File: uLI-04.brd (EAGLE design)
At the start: 57 x 38.5 mm, 39 parts, among them IC1 PIC18F14K50-I/SS, IC2 ADM2483, IC3 MCP130T, IC4 78L05F, J1 PICPROG2-V, J5 WEBP6-4, J6 WEBP6-4, J7 WEBP6-4, Q1 12.00 MHz, T1 IRF7306, X1 MINI-USB_SHIELD4P-USB-SPEC, X2 ARK1550/2_S

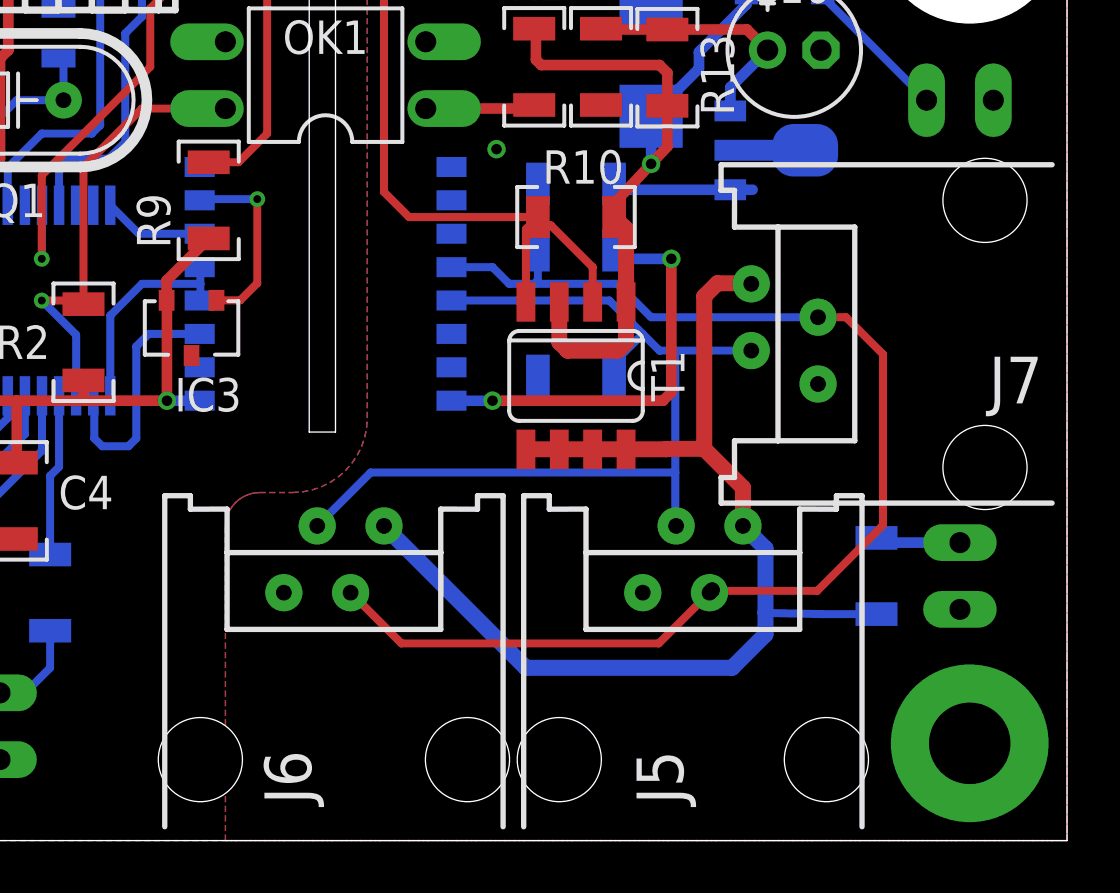
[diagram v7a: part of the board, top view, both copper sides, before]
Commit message: 6-4 > 6-6, ploska J5.
 * Konektory WEBP 6-4 nahrazeny za WEBP 6-6. Close #3.
 * Pajeci ploska pobliz J5 odstranena. Close 2.
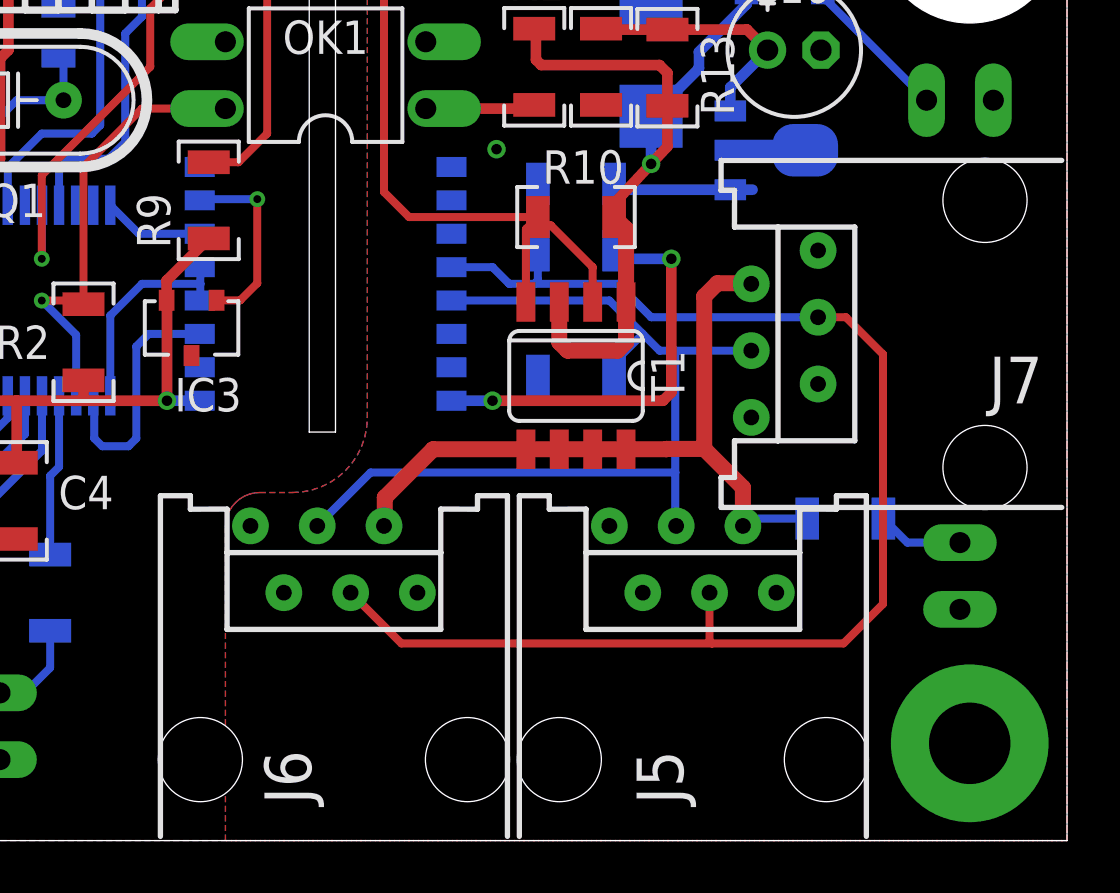
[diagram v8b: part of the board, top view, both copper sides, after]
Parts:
- J5, J6, J7: value WEBP6-4 -> WEBP6; device con-malina:WEBP6-4_SHORT -> con-malina:WEBP6-6_SPEC2
- moved R11 2.48 mm to (50.6, 14.2), turned to 0 degrees
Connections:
- new net N$11: J6.1
- new net N$12: J5.6
- new net N$13: J5.1
- new net N$14: J7.6
- new net N$15: J7.1
- new net N$8: J6.6
- net +NAP: now also J5.5, J6.5, J7.5; no longer J5.4, J6.4, J7.4
- net BUS_A: now also J5.4, J6.4, J7.4; no longer J5.3, J6.3, J7.3
- net BUS_B: now also J5.3, J6.3, J7.3; no longer J5.2, J6.2, J7.2
- net GNDINT: now also J5.2, J6.2, J7.2; no longer J5.1, J6.1, J7.1
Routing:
- net +NAP: track 44.1 -> 27.9 mm
- net BUS_A: track 48.7 -> 52.4 mm, vias 1 -> 0
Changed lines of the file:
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@@
 <attribute name="VALUE" x="46.339" y="34.0195" size="1.27" layer="27" ratio="10"/>
 </element>
-<element name="J5" library="con-malina" package="WEBP6-4_SHORT" value="WEBP6-4" x="44.7675" y="5.08" smashed="yes">
+<element name="J5" library="con-malina" package="WEBP6-6_SPEC2" value="WEBP6" x="44.7675" y="5.08" smashed="yes">
 <attribute name="NAME" x="44.4015" y="3.389" size="1.778" layer="25" rot="R90"/>
 </element>
-<element name="J6" library="con-malina" package="WEBP6-4_SHORT" value="WEBP6-4" x="31.115" y="5.08" smashed="yes">
+<element name="J6" library="con-malina" package="WEBP6-6_SPEC2" value="WEBP6" x="31.115" y="5.08" smashed="yes">
 <attribute name="NAME" x="30.249" y="3.389" size="1.778" layer="25" rot="R90"/>
 </element>
-<element name="J7" library="con-malina" package="WEBP6-4_SHORT" value="WEBP6-4" x="55.88" y="21.2725" smashed="yes" rot="R90">
+<element name="J7" library="con-malina" package="WEBP6-6_SPEC2" value="WEBP6" x="55.88" y="21.2725" smashed="yes" rot="R90">
 <attribute name="NAME" x="58.071" y="20.4065" size="1.778" layer="25" rot="R180"/>
 </element>
@@
 <attribute name="VALUE" x="58.7375" y="12.065" size="1.27" layer="28" ratio="15" rot="MR270" align="bottom-center"/>
 </element>
-<element name="R11" library="rcl" package="R1206" value="10k" x="51.7525" y="12.065" smashed="yes" rot="MR270">
-<attribute name="NAME" x="50.4825" y="13.335" size="1.27" layer="26" font="vector" ratio="15" rot="MR270"/>
-<attribute name="VALUE" x="50.2925" y="13.835" size="1.27" layer="28" font="vector" ratio="15" rot="MR270"/>
+<element name="R11" library="rcl" package="R1206" value="10k" x="50.565" y="14.2475" smashed="yes" rot="MR0">
+<attribute name="NAME" x="51.835" y="15.5175" size="1.27" layer="26" font="vector" ratio="15" rot="MR0"/>
+<attribute name="VALUE" x="52.335" y="15.7075" size="1.27" layer="28" font="vector" ratio="15" rot="MR0"/>
 </element>
 <element name="R13" library="rcl" package="R1206" value="22R" x="43.8" y="31.4" rot="R270"/>
@@
 <contactref element="X2" pad="2"/>
 <contactref element="LED5" pad="K"/>
-<contactref element="J6" pad="1"/>
-<contactref element="J7" pad="1"/>
-<contactref element="J5" pad="1"/>
+<contactref element="J6" pad="2"/>
+<contactref element="J7" pad="2"/>
+<contactref element="J5" pad="2"/>
 <via x="37.3" y="28.3" extent="1-16" drill="0.4"/>
 </signal>
@@
 <wire x1="38.8725" y1="24.4475" x2="38.8725" y2="23.315" width="0.3048" layer="16"/>
 <wire x1="38.8725" y1="23.315" x2="38.735" y2="23.1775" width="0.3048" layer="16"/>
-<contactref element="J6" pad="3"/>
-<contactref element="J7" pad="3"/>
-<contactref element="J5" pad="3"/>
+<contactref element="J6" pad="4"/>
+<contactref element="J7" pad="4"/>
+<contactref element="J5" pad="4"/>
 <wire x1="49.53" y1="21.9075" x2="43.18" y2="21.9075" width="0.3048" layer="16"/>
 <wire x1="31.75" y1="11.43" x2="33.68" y2="9.5" width="0.3048" layer="1"/>
-<wire x1="45.4025" y1="11.43" x2="43.4725" y2="9.5" width="0.3048" layer="1"/>
-<wire x1="43.4725" y1="9.5" x2="33.68" y2="9.5" width="0.3048" layer="1"/>
-<wire x1="45.4025" y1="11.43" x2="45.5" y2="11.5275" width="0.3048" layer="16"/>
+<wire x1="50.5" y1="9.5" x2="45.5" y2="9.5" width="0.3048" layer="1"/>
+<wire x1="45.5" y1="9.5" x2="33.68" y2="9.5" width="0.3048" layer="1"/>
 <wire x1="49.53" y1="21.73" x2="49.53" y2="21.9075" width="0.3048" layer="16"/>
-<via x="45.5" y="11.5275" extent="1-16" drill="0.6" shape="square"/>
-<wire x1="45.5" y1="11.5275" x2="45.5275" y2="11.5" width="0.3048" layer="1"/>
-<wire x1="45.5275" y1="11.5" x2="49.5" y2="11.5" width="0.3048" layer="1"/>
-<wire x1="49.5" y1="11.5" x2="52" y2="14" width="0.3048" layer="1"/>
-<wire x1="52" y1="14" x2="52" y2="20.5" width="0.3048" layer="1"/>
+<wire x1="52" y1="11" x2="52" y2="20.5" width="0.3048" layer="1"/>
 <wire x1="52" y1="20.5" x2="50.5925" y2="21.9075" width="0.3048" layer="1"/>
 <wire x1="50.5925" y1="21.9075" x2="49.53" y2="21.9075" width="0.3048" layer="1"/>
+<wire x1="50.5" y1="9.5" x2="52" y2="11" width="0.3048" layer="1"/>
+<wire x1="45.4025" y1="11.43" x2="45.4025" y2="9.5975" width="0.3048" layer="1"/>
+<wire x1="45.4025" y1="9.5975" x2="45.5" y2="9.5" width="0.3048" layer="1"/>
 </signal>
 <signal name="BUS_B" class="1">
@@
 <wire x1="41.7725" y1="19.685" x2="41.7725" y2="20.1825" width="0.3048" layer="16"/>
 <wire x1="41.7725" y1="20.1825" x2="42.8625" y2="21.2725" width="0.3048" layer="16"/>
-<contactref element="J6" pad="2"/>
-<contactref element="J7" pad="2"/>
-<contactref element="J5" pad="2"/>
+<contactref element="J6" pad="3"/>
+<contactref element="J7" pad="3"/>
+<contactref element="J5" pad="3"/>
 <wire x1="46.99" y1="20.6375" x2="44.1" y2="20.6375" width="0.3048" layer="16"/>
 <wire x1="44.1" y1="20.6375" x2="43.4975" y2="20.6375" width="0.3048" layer="16"/>
@@
 <contactref element="T1" pad="8"/>
 <contactref element="R11" pad="2"/>
-<wire x1="47.53" y1="10.66" x2="47.53" y2="9.8425" width="0.6096" layer="16"/>
-<wire x1="47.53" y1="9.8425" x2="46.26" y2="8.5725" width="0.6096" layer="16"/>
-<wire x1="51.7525" y1="10.615" x2="49.6675" y2="10.615" width="0.3048" layer="16"/>
-<wire x1="49.6675" y1="10.615" x2="47.53" y2="10.66" width="0.3048" layer="16"/>
 <wire x1="38.4175" y1="16.885" x2="39.6875" y2="16.885" width="0.6096" layer="1"/>
 <wire x1="39.6875" y1="16.885" x2="40.9575" y2="16.885" width="0.6096" layer="1"/>
 <wire x1="40.9575" y1="16.885" x2="42.2275" y2="16.885" width="0.6096" layer="1"/>
-<contactref element="J6" pad="4"/>
-<contactref element="J7" pad="4"/>
-<contactref element="J5" pad="4"/>
-<wire x1="46.26" y1="8.5725" x2="38.4175" y2="8.5725" width="0.6096" layer="16"/>
-<wire x1="38.4175" y1="8.5725" x2="33.02" y2="13.97" width="0.6096" layer="16"/>
-<wire x1="46.6725" y1="13.97" x2="47.53" y2="13.1125" width="0.6096" layer="16"/>
-<wire x1="47.53" y1="13.1125" x2="47.53" y2="10.66" width="0.6096" layer="16"/>
+<contactref element="J6" pad="5"/>
+<contactref element="J7" pad="5"/>
+<contactref element="J5" pad="5"/>
 <wire x1="43.7575" y1="16.885" x2="42.2275" y2="16.885" width="0.6096" layer="1"/>
 <wire x1="46.99" y1="23.1775" x2="46.9675" y2="23.2" width="0.6096" layer="1"/>
@@
 <wire x1="45.2" y1="16.9" x2="46.6725" y2="15.4275" width="0.6096" layer="1"/>
 <wire x1="46.6725" y1="15.4275" x2="46.6725" y2="13.97" width="0.6096" layer="1"/>
+<wire x1="33.05" y1="14" x2="33.05" y2="15.05" width="0.6096" layer="1"/>
+<wire x1="33.05" y1="15.05" x2="34.885" y2="16.885" width="0.6096" layer="1"/>
+<wire x1="38.4175" y1="16.885" x2="34.885" y2="16.885" width="0.6096" layer="1"/>
+<wire x1="49.115" y1="14.2475" x2="46.95" y2="14.2475" width="0.3048" layer="16"/>
+<wire x1="46.95" y1="14.2475" x2="46.6725" y2="13.97" width="0.3048" layer="16"/>
+<wire x1="33.05" y1="14" x2="33.02" y2="13.97" width="0" layer="19" extent="1-1"/>
 </signal>
 <signal name="N$1" class="1">
@@
 <contactref element="R11" pad="1"/>
 <contactref element="LED5" pad="A"/>
-<wire x1="51.9325" y1="13.335" x2="51.7525" y2="13.515" width="0.4064" layer="16"/>
-<wire x1="51.9325" y1="13.335" x2="54.9275" y2="13.335" width="0.4064" layer="16"/>
+<wire x1="54.9275" y1="13.335" x2="52.9275" y2="13.335" width="0.3048" layer="16"/>
+<wire x1="52.9275" y1="13.335" x2="52.015" y2="14.2475" width="0.3048" layer="16"/>
 </signal>
 <signal name="PV">
@@
 <wire x1="41.3075" y1="32.85" x2="41.275" y2="32.8825" width="0.4064" layer="1"/>
 </signal>
+<signal name="N$8" class="1">
+<contactref element="J6" pad="6"/>
+</signal>
+<signal name="N$11" class="1">
+<contactref element="J6" pad="1"/>
+</signal>
+<signal name="N$12" class="1">
+<contactref element="J5" pad="6"/>
+</signal>
+<signal name="N$13" class="1">
+<contactref element="J5" pad="1"/>
+</signal>
+<signal name="N$14" class="1">
+<contactref element="J7" pad="6"/>
+</signal>
+<signal name="N$15" class="1">
+<contactref element="J7" pad="1"/>
+</signal>
 </signals>
